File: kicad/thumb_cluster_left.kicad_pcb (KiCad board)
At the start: 2 copper layers, 41.2 x 46.6 mm, 18 parts, among them J1 Conn_01x07

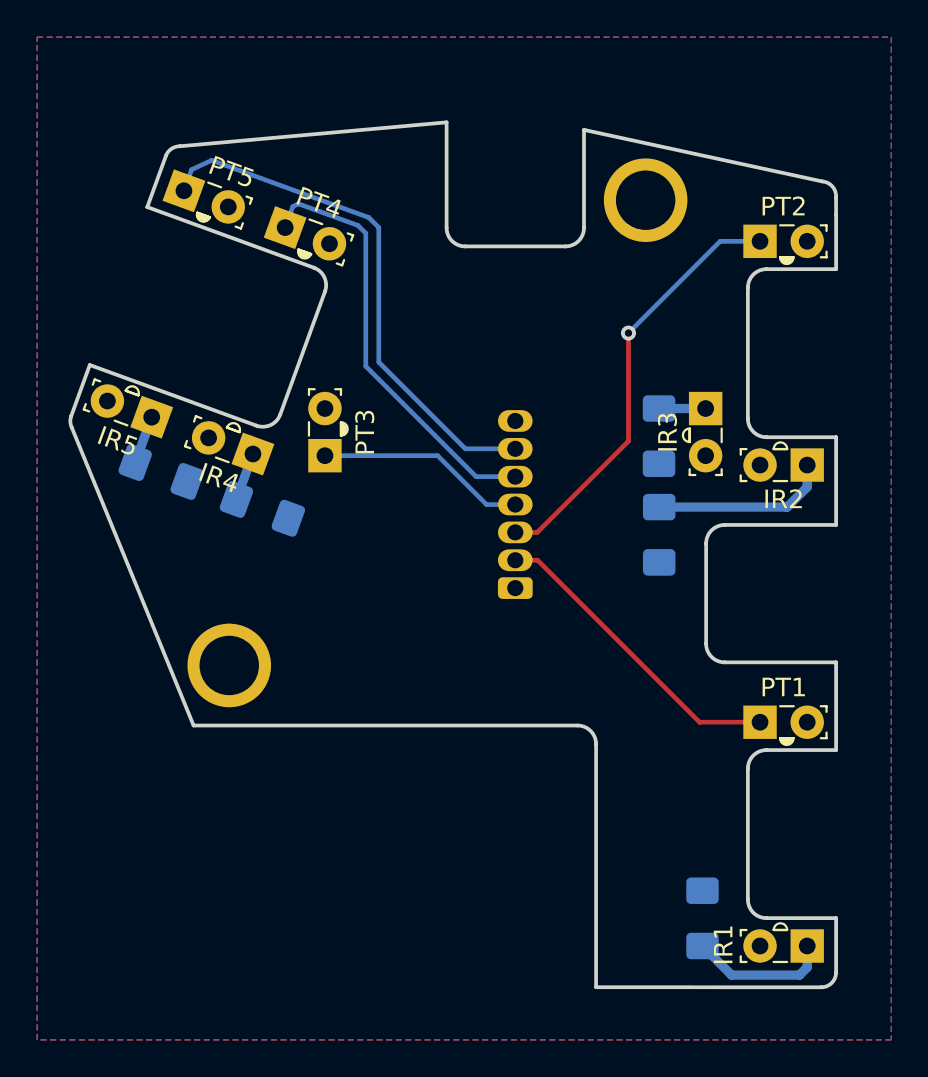
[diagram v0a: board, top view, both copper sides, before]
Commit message: Update kicad pcb data to change parts
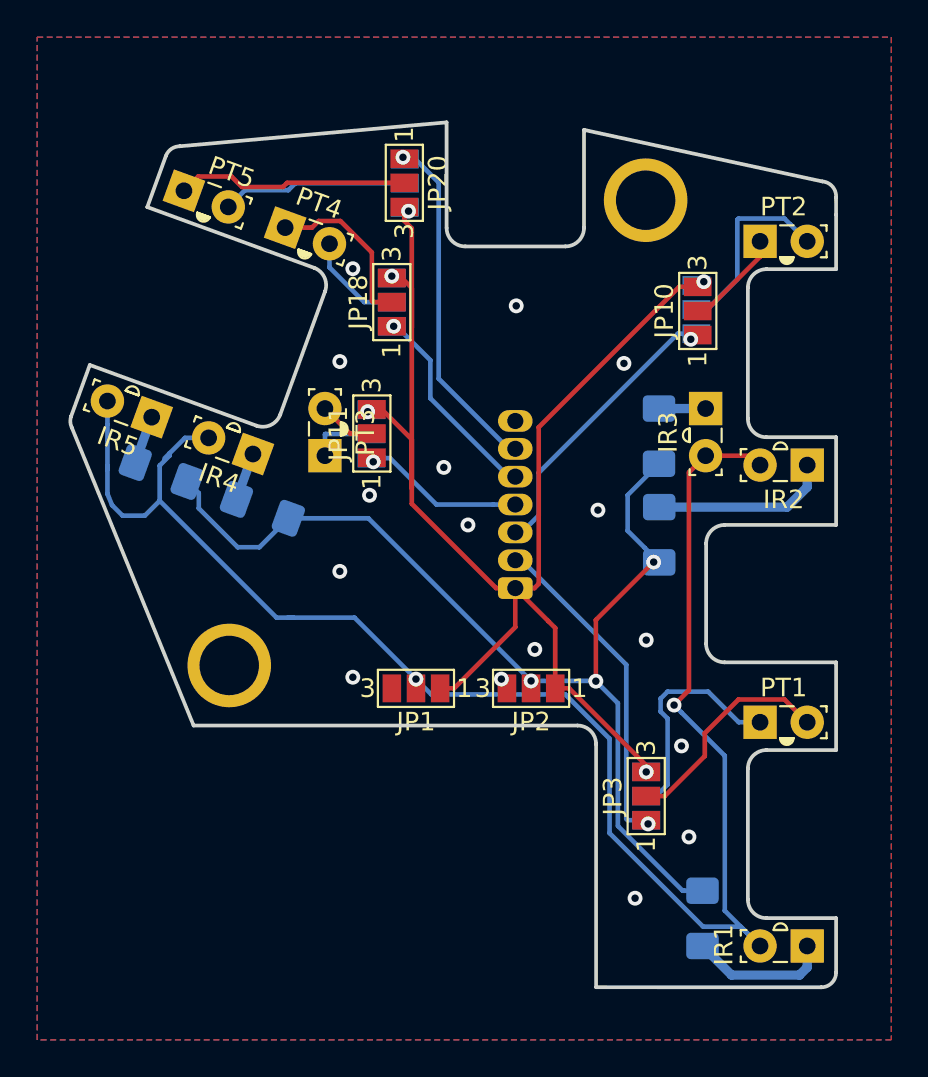
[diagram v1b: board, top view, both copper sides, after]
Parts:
- added JP1: SolderJumper_3_Open, Jumper:SolderJumper-3_P1.3mm_Open_Pad1.0x1.5mm_NumberLabels, F.Cu at (151.9, 92.6)
- added JP10: SolderJumper_3_Open, Jumper:SolderJumper-3_P1.3mm_Open_Pad1.0x1.5mm_NumberLabels, F.Cu at (167.1, 72.3)
- added JP11: SolderJumper_3_Open, Jumper:SolderJumper-3_P1.3mm_Open_Pad1.0x1.5mm_NumberLabels, F.Cu at (149.5, 78.9)
- added JP12: SolderJumper_3_Open, Jumper:SolderJumper-3_P1.3mm_Open_Pad1.0x1.5mm_NumberLabels, B.Cu at (149.5, 78.9)
- added JP17: SolderJumper_3_Open, Jumper:SolderJumper-3_P1.3mm_Open_Pad1.0x1.5mm_NumberLabels, B.Cu at (150.6, 71.8)
- added JP18: SolderJumper_3_Open, Jumper:SolderJumper-3_P1.3mm_Open_Pad1.0x1.5mm_NumberLabels, F.Cu at (150.6, 71.8)
- added JP19: SolderJumper_3_Open, Jumper:SolderJumper-3_P1.3mm_Open_Pad1.0x1.5mm_NumberLabels, B.Cu at (151.3, 65.4)
- added JP2: SolderJumper_3_Open, Jumper:SolderJumper-3_P1.3mm_Open_Pad1.0x1.5mm_NumberLabels, F.Cu at (158.1, 92.6)
- added JP20: SolderJumper_3_Open, Jumper:SolderJumper-3_P1.3mm_Open_Pad1.0x1.5mm_NumberLabels, F.Cu at (151.3, 65.4)
- added JP3: SolderJumper_3_Open, Jumper:SolderJumper-3_P1.3mm_Open_Pad1.0x1.5mm_NumberLabels, F.Cu at (164.3, 98.4)
- added JP4: SolderJumper_3_Open, Jumper:SolderJumper-3_P1.3mm_Open_Pad1.0x1.5mm_NumberLabels, B.Cu at (164.3, 98.4)
- added JP9: SolderJumper_3_Open, Jumper:SolderJumper-3_P1.3mm_Open_Pad1.0x1.5mm_NumberLabels, B.Cu at (167.0, 72.2)
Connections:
- IR1 pad 2: +5V -> /5VGND
- IR2 pad 2: +5V -> /5VGND
- IR3 pad 2: +5V -> /5VGND
- IR4 pad 2: +5V -> /5VGND
- IR5 pad 2: +5V -> /5VGND
- PT1 pad 1: C1 -> Net-(JP4-Pad2)
- PT1 pad 2: +5V -> Net-(JP3-Pad2)
- PT2 pad 1: C2 -> Net-(JP10-Pad2)
- PT2 pad 2: +5V -> Net-(JP9-Pad2)
- PT3 pad 1: C3 -> Net-(JP12-Pad2)
- PT3 pad 2: +5V -> Net-(JP11-Pad2)
- PT4 pad 1: C4 -> Net-(JP18-Pad2)
- PT4 pad 2: +5V -> Net-(JP17-Pad2)
- PT5 pad 1: C5 -> Net-(JP20-Pad2)
- PT5 pad 2: +5V -> Net-(JP19-Pad2)
- R1 pad 1: GND -> /GND5V
- R2 pad 1: GND -> /GND5V
- R3 pad 1: GND -> /GND5V
- R4 pad 1: GND -> /GND5V
- R5 pad 1: GND -> /GND5V
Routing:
- net /5VGND: track 0.00 -> 92.3 mm, vias 0 -> 2
- net +5V: track 0.00 -> 74.9 mm, vias 0 -> 5
- net /GND5V: track 0.00 -> 56.9 mm, vias 0 -> 3
- net Net-(JP20-Pad2): track 0.00 -> 13.1 mm
- net Net-(JP4-Pad2): track 0.00 -> 12.4 mm
- net Net-(JP3-Pad2): track 0.00 -> 12.1 mm
- net C4: track 23.2 -> 11.2 mm, vias 0 -> 1
- net Net-(JP9-Pad2): track 0.00 -> 10.4 mm
- net Net-(JP19-Pad2): track 0.00 -> 10.0 mm
- net C5: track 29.5 -> 19.5 mm, vias 0 -> 1
- net Net-(JP18-Pad2): track 0.00 -> 9.22 mm
- net C2: track 23.1 -> 15.5 mm
- net Net-(JP17-Pad2): track 0.00 -> 5.40 mm
- net Net-(JP10-Pad2): track 0.00 -> 5.39 mm
- net Net-(JP12-Pad2): track 0.00 -> 3.66 mm
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- added copper zone on F.Cu, net GND
- removed copper zone on F.Cu, net +5V

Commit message: Customize
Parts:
- removed IR3: IR908-7C-F, lalboard:IR908-7C-F
- removed JP11, JP12: SolderJumper_3_Open, Jumper:SolderJumper-3_P1.3mm_Open_Pad1.0x1.5mm_NumberLabels
- removed PT3: PT908-7B-F, lalboard:PT908-7C-F
- added SW1: D2FS-F-N, lalboard:Omron-D2FS-F-N-MFG, B.Cu at (157.1, 73.1)
- added SW2: SW_Push, lalboard:CMI625501D06, B.Cu at (154.8, 73.1)
- R3: value 120 -> 5.1k
- moved JP17 3.81 mm to (148.7, 75.1)
- moved JP18 3.81 mm to (148.7, 75.1)
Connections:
- R3 pad 1: /GND5V -> C3
- R3 pad 2: Net-(IR3-Pad1) -> +5V
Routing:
- net C3: track 8.79 -> 25.0 mm, vias 1 -> 0
- net /GND5V: track 56.9 -> 50.2 mm
- net Net-(JP17-Pad2): track 5.40 -> 9.27 mm
- net Net-(JP12-Pad2): track 3.66 -> 0.00 mm
- net Net-(JP18-Pad2): track 9.22 -> 12.6 mm
- net Net-(JP11-Pad2): track 3.08 -> 0.00 mm
- net C2: track 15.5 -> 18.6 mm
- net Net-(IR3-Pad1): track 2.51 -> 0.00 mm
- net +5V: track 74.9 -> 73.9 mm, vias 5 -> 6
- net C4: track 11.2 -> 10.5 mm
- net GND: vias 16 -> 17
